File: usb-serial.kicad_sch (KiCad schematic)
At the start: 31 parts, among them J11 Connector, USB-TYPE-C-16P, J12 Connector, USB-TYPE-C-16P, Q10 Q_NPN, Q11 Q_NPN, U6 CP2102N-Axx-xQFN28

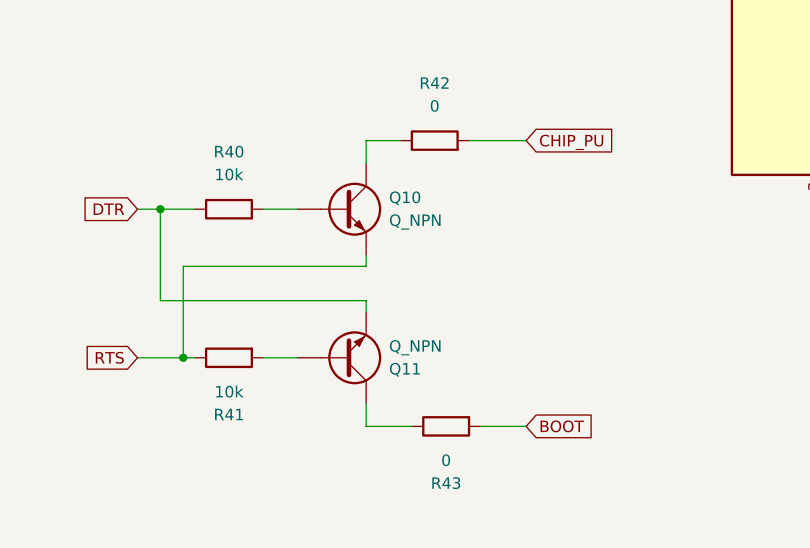
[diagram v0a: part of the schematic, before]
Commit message: added usb-serial programmer and footprints
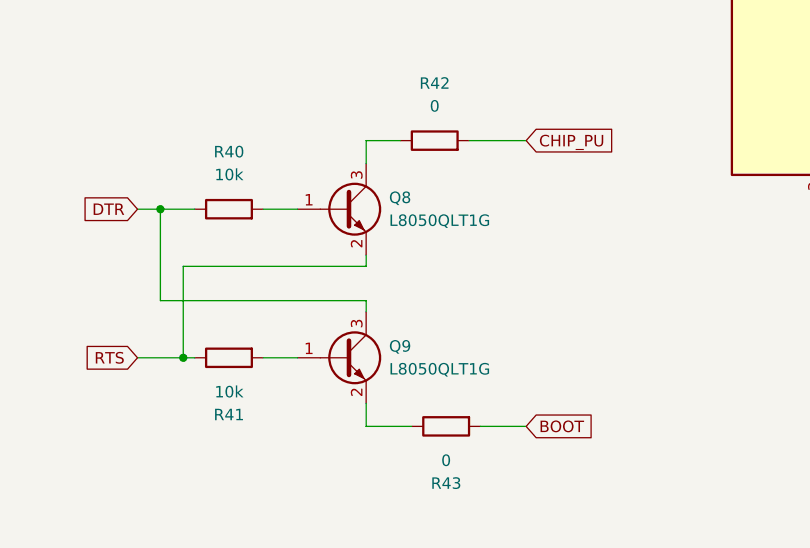
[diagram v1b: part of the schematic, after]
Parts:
- removed Q10, Q11: Q_NPN, symbol Device:Q_NPN
- added Q8, Q9: L8050QLT1G, Package_TO_SOT_SMD:SOT-23, symbol Transistor_BJT:2SC4213
- C11, C12, C14: footprint (none) -> PCM_JLCPCB:C_0805
- C13: footprint (none) -> PCM_JLCPCB:C_0603
- R35, R36, R37, R40, R41: footprint (none) -> PCM_JLCPCB:R_0603
- R38, R39, R42, R43: footprint (none) -> PCM_JLCPCB:R_0805
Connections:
- net DTR: now also Q9.3 (C)
- net RTS: now also Q8.2 (E)
- net at R41.2: now also Q9.1 (B)
- net at R43.1: now also Q9.2 (E)
- net at R40.2: now also Q8.1 (B)
- net at R42.1: now also Q8.3 (C)
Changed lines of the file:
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@@
 			)
 		)
-		(property "Footprint" ""
+		(property "Footprint" "PCM_JLCPCB:R_0805"
 			(at 248.92 60.452 90)
 			(hide yes)
@@
 			)
 		)
-		(property "Footprint" ""
+		(property "Footprint" "PCM_JLCPCB:C_0805"
 			(at 214.3252 44.45 0)
 			(hide yes)
@@
 	)
 	(symbol
-		(lib_id "Device:Q_NPN")
-		(at 170.18 138.43 0)
-		(mirror x)
-		(unit 1)
-		(body_style 1)
-		(exclude_from_sim no)
-		(in_bom yes)
-		(on_board yes)
-		(in_pos_files yes)
-		(dnp no)
-		(property "Reference" "Q11"
-			(at 175.26 139.7001 0)
-			(show_name no)
-			(do_not_autoplace no)
-			(effects
-				(font
-					(size 1.27 1.27)
-				)
-				(justify left)
-			)
-		)
-		(property "Value" "Q_NPN"
-			(at 175.26 137.1601 0)
-			(show_name no)
-			(do_not_autoplace no)
-			(effects
-				(font
-					(size 1.27 1.27)
-				)
-				(justify left)
-			)
-		)
-		(property "Footprint" ""
-			(at 175.26 140.97 0)
-			(hide yes)
-			(show_name no)
-			(do_not_autoplace no)
-			(effects
-				(font
-					(size 1.27 1.27)
-				)
-			)
-		)
-		(property "Datasheet" ""
-			(at 170.18 138.43 0)
-			(hide yes)
-			(show_name no)
-			(do_not_autoplace no)
-			(effects
-				(font
-					(size 1.27 1.27)
-				)
-			)
-		)
-		(property "Description" "NPN bipolar junction transistor"
-			(at 170.18 138.43 0)
-			(hide yes)
-			(show_name no)
-			(do_not_autoplace no)
-			(effects
-				(font
-					(size 1.27 1.27)
-				)
-			)
-		)
-		(pin "E"
-		)
-		(pin "C"
-		)
-		(pin "B"
-		)
-		(instances
-			(project "presstimer"
-				(path "/63494a82-20b5-470b-977d-6a82bfa70174/0171fa45-2753-4764-a2d1-635868f3d686"
-					(reference "Q11")
-					(unit 1)
-				)
-			)
-		)
-	)
-	(symbol
 		(lib_id "Device:R")
 		(at 248.92 59.69 90)
@@
 			)
 		)
-		(property "Footprint" ""
+		(property "Footprint" "PCM_JLCPCB:R_0805"
 			(at 248.92 61.468 90)
 			(hide yes)
@@
 			)
 		)
-		(property "Footprint" ""
+		(property "Footprint" "PCM_JLCPCB:C_0603"
 			(at 188.9252 83.82 0)
 			(hide yes)
@@
 			)
 		)
-		(property "Footprint" ""
+		(property "Footprint" "PCM_JLCPCB:R_0603"
 			(at 157.48 123.698 90)
 			(hide yes)
@@
 			)
 		)
-		(property "Footprint" ""
+		(property "Footprint" "PCM_JLCPCB:R_0805"
 			(at 181.61 144.272 90)
 			(hide yes)
@@
 	)
 	(symbol
-		(lib_id "Device:R")
-		(at 181.61 80.01 0)
-		(mirror y)
+		(lib_id "Transistor_BJT:2SC4213")
+		(at 170.18 138.43 0)
 		(unit 1)
 		(body_style 1)
@@
 		(in_pos_files yes)
 		(dnp no)
-		(property "Reference" "R36"
-			(at 179.07 78.7399 0)
+		(fields_autoplaced yes)
+		(property "Reference" "Q9"
+			(at 175.26 137.1599 0)
 			(show_name no)
 			(do_not_autoplace no)
@@
 			)
 		)
-		(property "Value" "47k5"
-			(at 179.07 81.2799 0)
+		(property "Value" "L8050QLT1G"
+			(at 175.26 139.6999 0)
 			(show_name no)
 			(do_not_autoplace no)
@@
 			)
 		)
-		(property "Footprint" ""
-			(at 183.388 80.01 90)
+		(property "Footprint" "Package_TO_SOT_SMD:SOT-23"
+			(at 175.26 140.335 0)
 			(hide yes)
 			(show_name no)
@@
 				(font
 					(size 1.27 1.27)
+					(italic yes)
 				)
+				(justify left)
 			)
 		)
-		(property "Datasheet" ""
-			(at 181.61 80.01 0)
+		(property "Datasheet" "https://www.lcsc.com/datasheet/C49581.pdf"
+			(at 170.18 138.43 0)
 			(hide yes)
 			(show_name no)
@@
 					(size 1.27 1.27)
 				)
+				(justify left)
 			)
 		)
-		(property "Description" "Resistor"
-			(at 181.61 80.01 0)
+		(property "Description" "TRANS NPN 25V 800mA SOT-23"
+			(at 170.18 138.43 0)
+			(hide yes)
+			(show_name no)
+			(do_not_autoplace no)
+			(effects
+				(font
+					(size 1.27 1.27)
+				)
+			)
+		)
+		(property "Sim.Device" "NPN"
+			(at 170.18 138.43 0)
+			(hide yes)
+			(show_name no)
+			(do_not_autoplace no)
+			(effects
+				(font
+					(size 1.27 1.27)
+				)
+			)
+		)
+		(property "Sim.Pins" "1=B 2=E 3=C"
+			(at 170.18 138.43 0)
 			(hide yes)
 			(show_name no)
@@
 		(pin "2"
 		)
+		(pin "3"
+		)
 		(instances
 			(project "presstimer"
 				(path "/63494a82-20b5-470b-977d-6a82bfa70174/0171fa45-2753-4764-a2d1-635868f3d686"
-					(reference "R36")
+					(reference "Q9")
 					(unit 1)
 				)
@@
 	)
 	(symbol
-		(lib_id "Device:Q_NPN")
-		(at 170.18 121.92 0)
+		(lib_id "Device:R")
+		(at 181.61 80.01 0)
+		(mirror y)
 		(unit 1)
 		(body_style 1)
@@
 		(in_pos_files yes)
 		(dnp no)
-		(fields_autoplaced yes)
-		(property "Reference" "Q10"
-			(at 175.26 120.6499 0)
+		(property "Reference" "R36"
+			(at 179.07 78.7399 0)
 			(show_name no)
 			(do_not_autoplace no)
@@
 			)
 		)
-		(property "Value" "Q_NPN"
-			(at 175.26 123.1899 0)
+		(property "Value" "47k5"
+			(at 179.07 81.2799 0)
 			(show_name no)
 			(do_not_autoplace no)
@@
 			)
 		)
-		(property "Footprint" ""
-			(at 175.26 119.38 0)
+		(property "Footprint" "PCM_JLCPCB:R_0603"
+			(at 183.388 80.01 90)
 			(hide yes)
 			(show_name no)
@@
 		)
 		(property "Datasheet" ""
-			(at 170.18 121.92 0)
+			(at 181.61 80.01 0)
 			(hide yes)
 			(show_name no)
@@
 			)
 		)
-		(property "Description" "NPN bipolar junction transistor"
-			(at 170.18 121.92 0)
+		(property "Description" "Resistor"
+			(at 181.61 80.01 0)
 			(hide yes)
 			(show_name no)
@@
 			)
 		)
-		(pin "E"
-		)
-		(pin "C"
+		(pin "1"
 		)
-		(pin "B"
+		(pin "2"
 		)
 		(instances
 			(project "presstimer"
 				(path "/63494a82-20b5-470b-977d-6a82bfa70174/0171fa45-2753-4764-a2d1-635868f3d686"
-					(reference "Q10")
+					(reference "R36")
 					(unit 1)
 				)
@@
 			)
 		)
-		(property "Footprint" ""
+		(property "Footprint" "PCM_JLCPCB:R_0603"
 			(at 173.99 74.168 90)
 			(hide yes)
@@
 			)
 		)
-		(property "Footprint" ""
+		(property "Footprint" "PCM_JLCPCB:R_0805"
 			(at 180.34 116.078 90)
 			(hide yes)
@@
 			)
 		)
-		(property "Footprint" ""
+		(property "Footprint" "PCM_JLCPCB:C_0805"
 			(at 121.6152 62.23 0)
 			(hide yes)
@@
 			)
 		)
-		(property "Footprint" ""
+		(property "Footprint" "PCM_JLCPCB:C_0805"
 			(at 120.3452 132.08 0)
 			(hide yes)
@@
 			)
 		)
-		(property "Footprint" ""
+		(property "Footprint" "PCM_JLCPCB:R_0603"
 			(at 157.48 136.652 90)
 			(hide yes)
@@
 			)
 		)
-		(property "Footprint" ""
+		(property "Footprint" "PCM_JLCPCB:R_0603"
 			(at 203.2 61.468 90)
 			(hide yes)
@@
 					(unit 1)
 				)
+			)
+		)
+	)
+	(symbol
+		(lib_id "Transistor_BJT:2SC4213")
+		(at 170.18 121.92 0)
+		(unit 1)
+		(body_style 1)
+		(exclude_from_sim no)
+		(in_bom yes)
+		(on_board yes)
+		(in_pos_files yes)
+		(dnp no)
+		(fields_autoplaced yes)
+		(property "Reference" "Q8"
+			(at 175.26 120.6499 0)
+			(show_name no)
+			(do_not_autoplace no)
+			(effects
+				(font
+					(size 1.27 1.27)
+				)
+				(justify left)
+			)
+		)
+		(property "Value" "L8050QLT1G"
+			(at 175.26 123.1899 0)
+			(show_name no)
+			(do_not_autoplace no)
+			(effects
+				(font
+					(size 1.27 1.27)
+				)
+				(justify left)
+			)
+		)
+		(property "Footprint" "Package_TO_SOT_SMD:SOT-23"
+			(at 175.26 123.825 0)
+			(hide yes)
+			(show_name no)
+			(do_not_autoplace no)
+			(effects
+				(font
+					(size 1.27 1.27)
+					(italic yes)
+				)
+				(justify left)
+			)
+		)
+		(property "Datasheet" "https://www.lcsc.com/datasheet/C49581.pdf"
+			(at 170.18 121.92 0)
+			(hide yes)
+			(show_name no)
+			(do_not_autoplace no)
+			(effects
+				(font
+					(size 1.27 1.27)
+				)
+				(justify left)
+			)
+		)
+		(property "Description" "TRANS NPN 25V 800mA SOT-23"
+			(at 170.18 121.92 0)
+			(hide yes)
+			(show_name no)
+			(do_not_autoplace no)
+			(effects
+				(font
+					(size 1.27 1.27)
+				)
+			)
+		)
+		(property "Sim.Device" "NPN"
+			(at 170.18 121.92 0)
+			(hide yes)
+			(show_name no)
+			(do_not_autoplace no)
+			(effects
+				(font
+					(size 1.27 1.27)
+				)
+			)
+		)
+		(property "Sim.Pins" "1=B 2=E 3=C"
+			(at 170.18 121.92 0)
+			(hide yes)
+			(show_name no)
+			(do_not_autoplace no)
+			(effects
+				(font
+					(size 1.27 1.27)
+				)
+			)
+		)
+		(pin "1"
+		)
+		(pin "2"
+		)
+		(pin "3"
+		)
+		(instances
+			(project "presstimer"
+				(path "/63494a82-20b5-470b-977d-6a82bfa70174/0171fa45-2753-4764-a2d1-635868f3d686"
+					(reference "Q8")
+					(unit 1)
+				)
